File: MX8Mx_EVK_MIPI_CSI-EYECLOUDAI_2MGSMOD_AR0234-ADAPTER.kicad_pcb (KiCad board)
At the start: 2 copper layers, 40.5 x 40.5 mm, 8 parts, among them J1 1888863-4, J2 3-1734592-0, J3 53261-0271

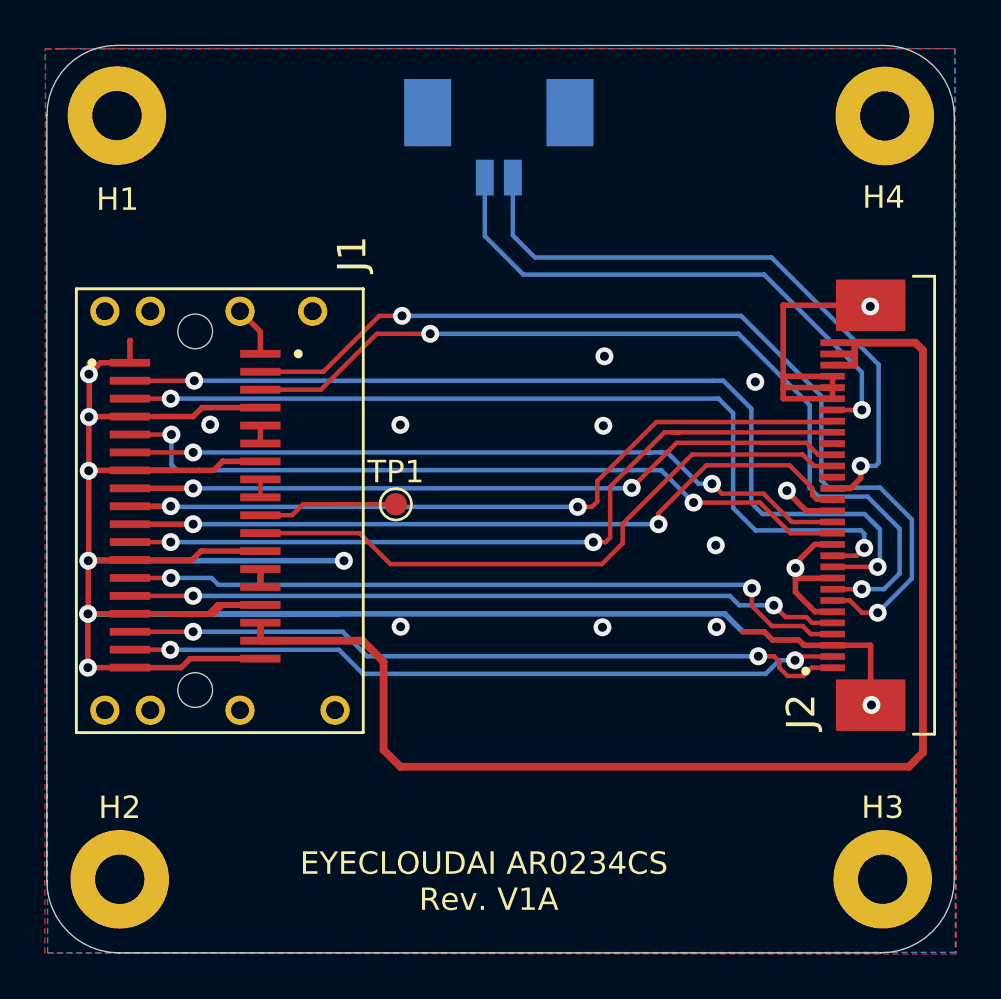
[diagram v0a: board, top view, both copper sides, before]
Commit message: Add more testpoints
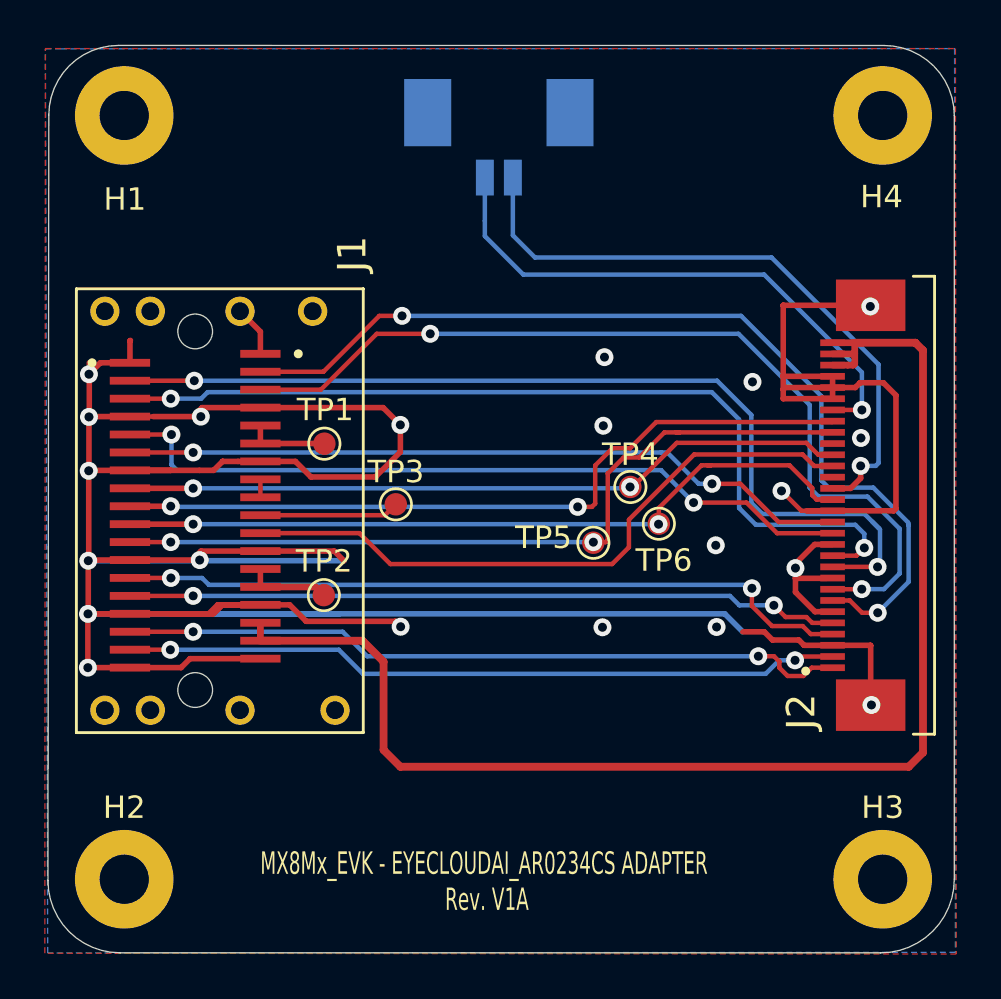
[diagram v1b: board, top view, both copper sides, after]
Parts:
- added TP1: TestPoint, TestPoint:TestPoint_Pad_D1.0mm, F.Cu at (114.6, 93.8)
- added TP2: TestPoint, TestPoint:TestPoint_Pad_D1.0mm, F.Cu at (114.6, 100.6)
- added TP4: TestPoint, TestPoint:TestPoint_Pad_D1.0mm, F.Cu at (128.3, 95.7)
- added TP5: TestPoint, TestPoint:TestPoint_Pad_D1.0mm, F.Cu at (126.6, 98.2)
- added TP6: TestPoint, TestPoint:TestPoint_Pad_D1.0mm, F.Cu at (129.6, 97.4)
- moved H1 0.33 mm to (105.7, 79.2)
- moved H2 0.20 mm to (105.7, 113.2)
- moved H4 0.10 mm to (139.6, 79.2)
- renumbered TP1 to TP3
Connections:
- net /CLK_SI_3V3 renamed /CSI_MCLK_1V8
- net /I2C_CLK_3V3 renamed /I2C_SCL_1V8
- net /I2C_DAT_3V3 renamed /I2C_SDA_1V8
- net Net-(J1-PadB5) renamed /+1V8
- net Net-(J1-PadB8) renamed /+12V
- J1 pad B13: Net-(J1-PadB13) -> /+3V3
- J1 pad B14: Net-(J1-PadB14) -> /+3V3
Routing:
- net GND: track 150.5 -> 188.5 mm, vias 20 -> 21
- net /+3V3: track 0.00 -> 3.78 mm
- net /+1V8: track 0.80 -> 3.66 mm
- net +3V3: track 0.80 -> 0.00 mm
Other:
- board size 40.5 x 40.5 mm -> 40.4 x 40.5 mm
- board text added: "MX8Mx_EVK - EYECLOUDAI_AR0234CS ADAPTER Rev. V1A"
- board text removed: "EYECLOUDAI AR0234CS Rev. V1A"
